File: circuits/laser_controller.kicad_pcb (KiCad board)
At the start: 4 copper layers, 173 x 61.1 mm, 178 parts, among them J1 USB_MINI_B, J2 USB_MINI_B, J5 24V DC IN, J6 CONN_RJ45, Q1 SOT-23, Q2 SOT-23, Q3 SOT-23, Q4 SOT-23, Q5 SOT-23, Q6 SOT-23, SW1 SW_PUSH, SW2 SW_PUSH, SW3 SW_PUSH, U1 SOIC-8_3.9x4.9mm_P1.27mm, U10 QFN-28-1EP_5x5mm_P0.5mm_EP3.3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, U11 SOT-23-5, U12 TSSOP-14_4.4x5mm_P0.65mm, U13 SOT-23, U14 LQFP-64_10x10mm_P0.5mm, U15 TSOT-23-6, U16 TSOT-23-6, U2 SOIC-8_3.9x4.9mm_P1.27mm, U3 SOIC-8_3.9x4.9mm_P1.27mm, U4 SOIC-8_3.9x4.9mm_P1.27mm, U5 SOT-23-5, U6 SOT-23-5, U7 SOT-23-5, U8 SOT-23-5, U9 ESP32-S3-WROOM-1

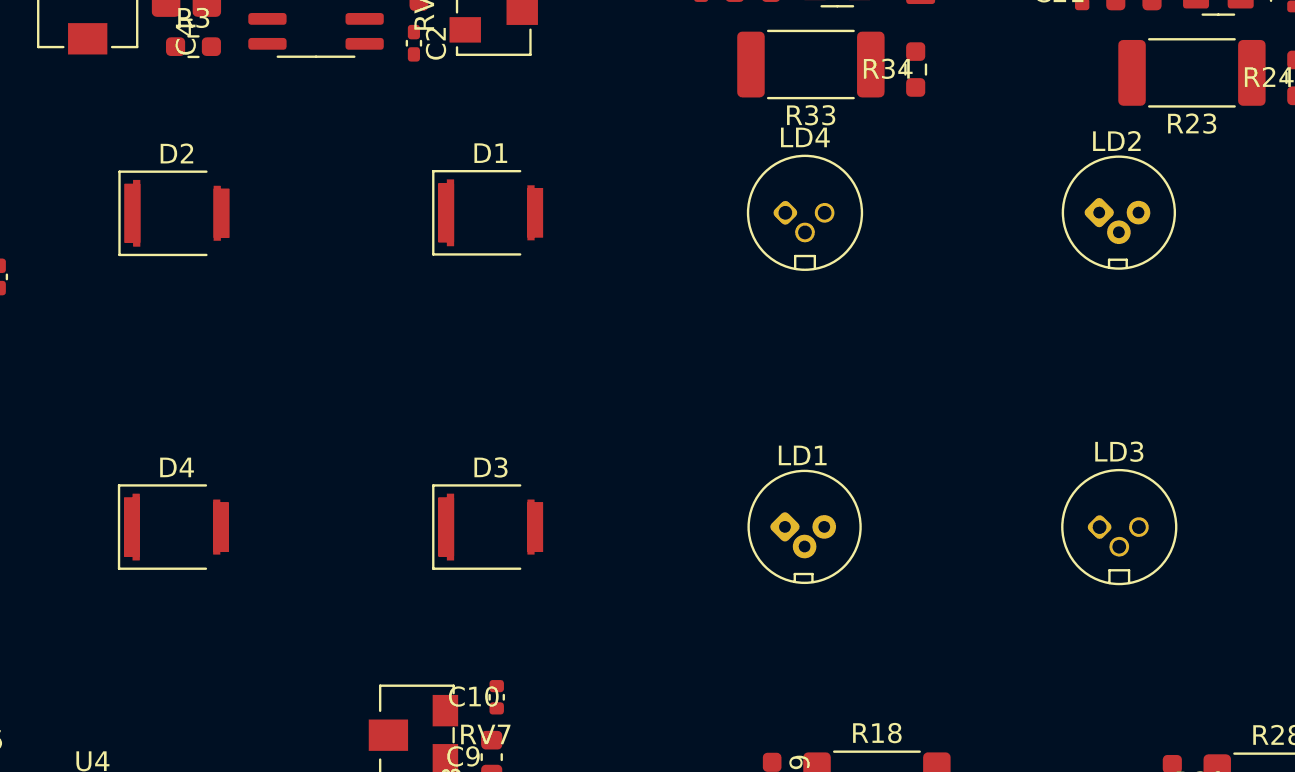
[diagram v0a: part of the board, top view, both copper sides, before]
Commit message: Center PDs and lasers on board Y axis (16mm spacing, symmetric about y=110.44)
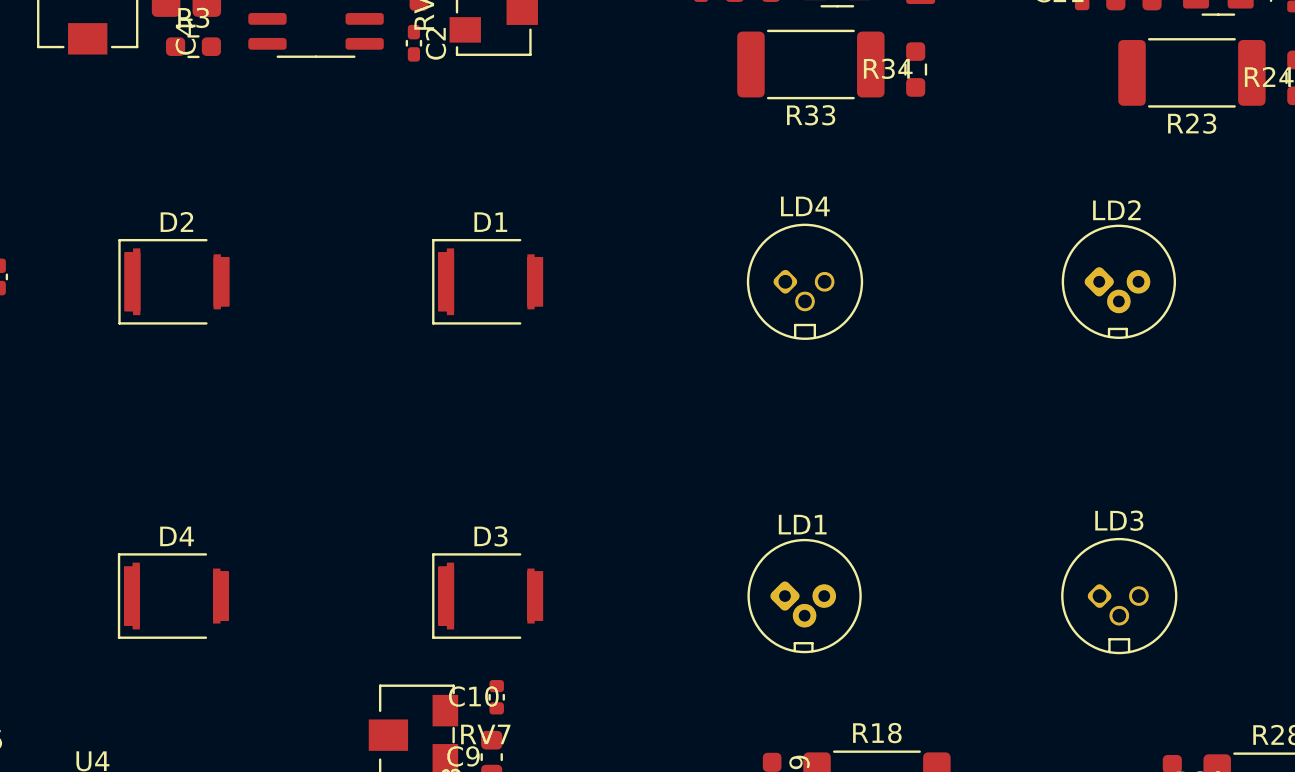
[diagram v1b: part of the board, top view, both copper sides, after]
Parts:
- moved LD1 3.52 mm to (168.9, 118.4)
- moved LD2 3.52 mm to (184.9, 102.4)
- moved D1 3.51 mm to (153.9, 102.4)
- moved D3 3.51 mm to (153.9, 118.4)
- moved D4 3.51 mm to (137.9, 118.4)
- moved LD3 3.51 mm to (184.9, 118.4)
- moved LD4 3.51 mm to (168.9, 102.4)
- moved D2 3.49 mm to (137.9, 102.4)
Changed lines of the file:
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@@
   (net 119 "VOUT4")
   (footprint "Osram_SFH2201" (layer "F.Cu")
-    (at 153.9 98.925)
+    (at 153.9 102.4375)
     (descr "PhotoDiode, Clear Silicone, Osram TOPLED, 4x5.09mm, area: 2.85x2.85mm, Orientation mark at cathode, https://dammedia.osram.info/media/resource/hires/osram-dam-25688470/SFH%202201%20A01_EN.pdf")
     (tags "PhotoDiode silicone")
@@
   )
   (footprint "Osram_SFH2201" (layer "F.Cu")
-    (at 137.925 98.95)
+    (at 137.925 102.4375)
     (descr "PhotoDiode, Clear Silicone, Osram TOPLED, 4x5.09mm, area: 2.85x2.85mm, Orientation mark at cathode, https://dammedia.osram.info/media/resource/hires/osram-dam-25688470/SFH%202201%20A01_EN.pdf")
     (tags "PhotoDiode silicone")
@@
   )
   (footprint "Osram_SFH2201" (layer "F.Cu")
-    (at 153.9 114.925)
+    (at 153.9 118.4375)
     (descr "PhotoDiode, Clear Silicone, Osram TOPLED, 4x5.09mm, area: 2.85x2.85mm, Orientation mark at cathode, https://dammedia.osram.info/media/resource/hires/osram-dam-25688470/SFH%202201%20A01_EN.pdf")
     (tags "PhotoDiode silicone")
@@
   )
   (footprint "Osram_SFH2201" (layer "F.Cu")
-    (at 137.9 114.925)
+    (at 137.9 118.4375)
     (descr "PhotoDiode, Clear Silicone, Osram TOPLED, 4x5.09mm, area: 2.85x2.85mm, Orientation mark at cathode, https://dammedia.osram.info/media/resource/hires/osram-dam-25688470/SFH%202201%20A01_EN.pdf")
     (tags "PhotoDiode silicone")
@@
   )
   (footprint "LaserDiode_TO18-D5.6-3" (layer "F.Cu")
-    (at 168.88 114.915)
+    (at 168.88 118.4375)
     (descr "Laser Diode, TO18-like (D=5.6mm), 3pin")
     (tags "Laser Diode TO18-like")
@@
   )
   (footprint "LaserDiode_TO18-D5.6-3" (layer "F.Cu")
-    (at 184.88 98.915)
+    (at 184.88 102.4375)
     (descr "Laser Diode, TO18-like (D=5.6mm), 3pin")
     (tags "Laser Diode TO18-like")
@@
   )
   (footprint "LaserDiode_TO56-3" (layer "F.Cu")
-    (at 184.9 114.925)
+    (at 184.9 118.4375)
     (descr "Laser Diode, TO-56, 3pin")
     (tags "Laser Diode TO56")
@@
   )
   (footprint "LaserDiode_TO56-3" (layer "F.Cu")
-    (at 168.9 98.925)
+    (at 168.9 102.4375)
     (descr "Laser Diode, TO-56, 3pin")
     (tags "Laser Diode TO56")

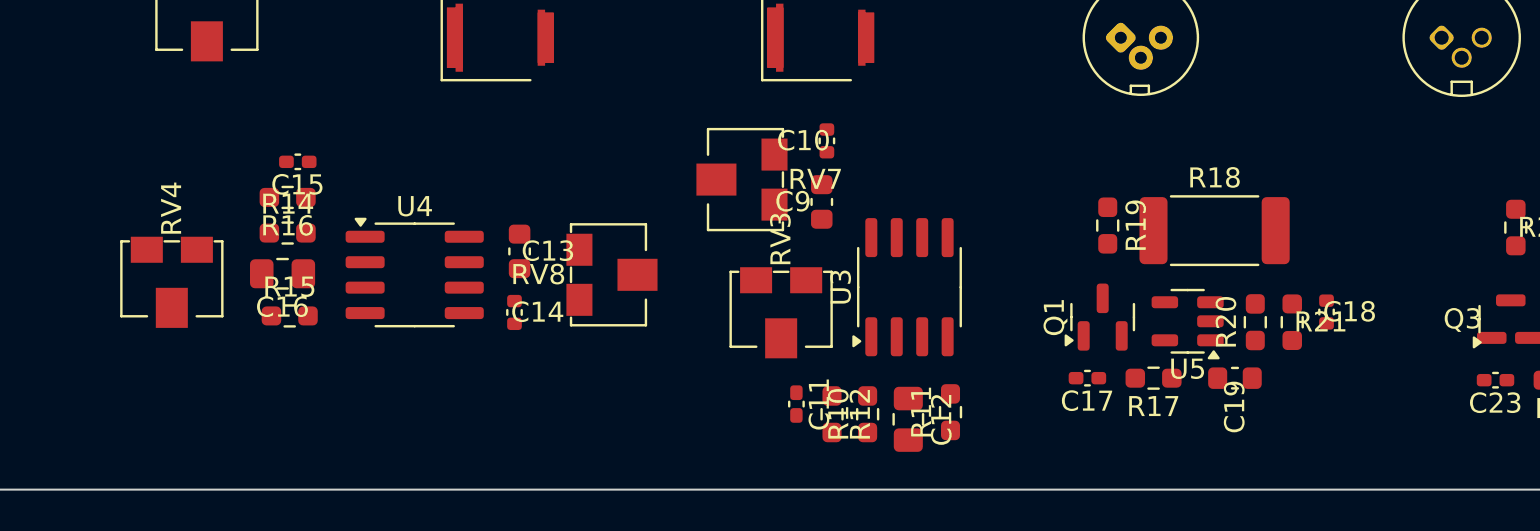
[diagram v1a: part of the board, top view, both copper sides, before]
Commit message: Rotate laser controller backups and sync latest PCB state
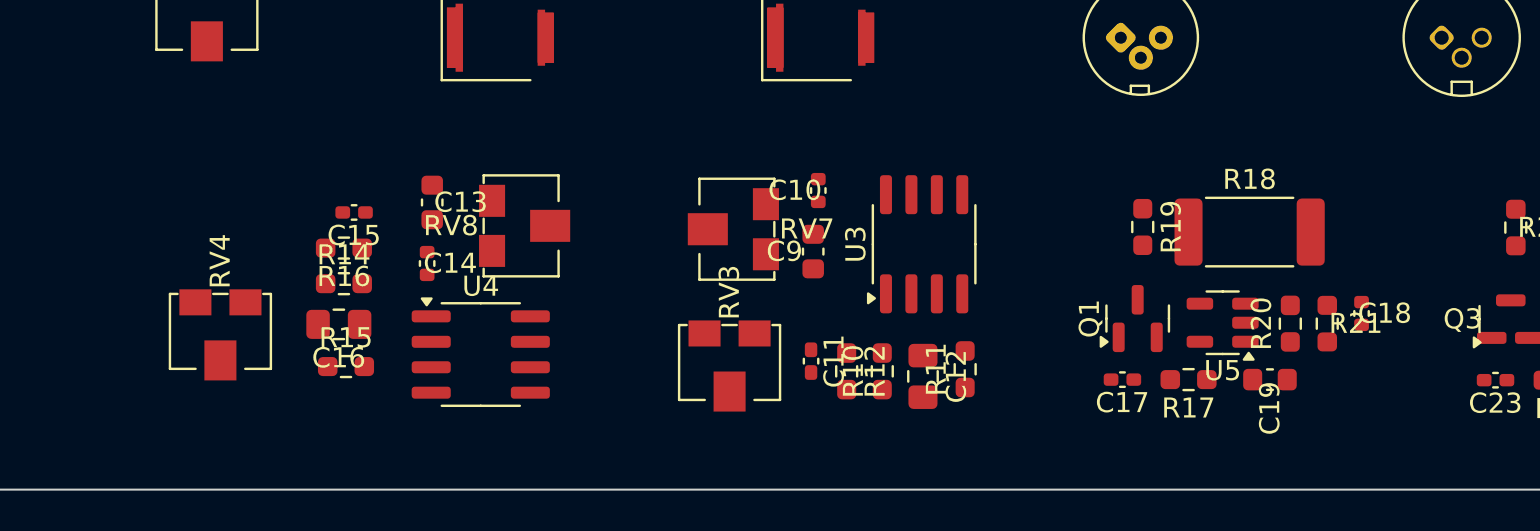
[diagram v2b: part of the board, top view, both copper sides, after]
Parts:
- moved U4 5.17 mm to (136.9, 134.3)
- moved RV8 5.00 mm to (138.9, 127.8)
- moved C13 5.00 mm to (134.5, 126.7)
- moved C14 5.00 mm to (134.2, 129.7)
- moved C15 3.78 mm to (130.6, 127.2)
- moved C16 3.78 mm to (129.8, 132.8)
- moved R14 3.78 mm to (130.1, 130.7)
- moved R16 3.78 mm to (130.1, 128.9)
- moved R15 3.78 mm to (130.2, 134.9)
- moved RV3 3.70 mm to (149.3, 134.7)
- moved RV4 3.57 mm to (123.9, 133.1)
- moved C10 2.51 mm to (153.8, 126.1)
- moved C9 2.51 mm to (153.5, 129.1)
- moved RV7 2.51 mm to (149.7, 128.0)
- moved C11 2.26 mm to (153.4, 134.6)
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
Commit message: Add 3x M3 mounting holes (GND, 3.2mm drill, 7mm pad) for case mounting
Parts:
- added H1: M3, MountingHole_3.2mm_M3, F.Cu at (84.0, 85.0)
- added H2: M3, MountingHole_3.2mm_M3, F.Cu at (197.0, 109.0)
- added H3: M3, MountingHole_3.2mm_M3, F.Cu at (117.0, 136.0)
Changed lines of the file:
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@@
     )
+  )
+  (footprint "MountingHole_3.2mm_M3" (layer "F.Cu")
+    (at 84 85)
+    (attr through_hole)
+    (fp_text reference "H1" (at 0 4.5) (layer "F.SilkS")
+        (effects (font (size 1 1) (thickness 0.15)))
+    )
+    (fp_text value "M3" (at 0 -4.5) (layer "F.Fab")
+        (effects (font (size 1 1) (thickness 0.15)))
+    )
+    (pad "1" thru_hole circle (at 0 0) (size 7 7) (drill 3.2) (layers "*.Cu" "*.Mask")
+      (net 46 "GND"))
+  )
+  (footprint "MountingHole_3.2mm_M3" (layer "F.Cu")
+    (at 197 109)
+    (attr through_hole)
+    (fp_text reference "H2" (at 0 4.5) (layer "F.SilkS")
+        (effects (font (size 1 1) (thickness 0.15)))
+    )
+    (fp_text value "M3" (at 0 -4.5) (layer "F.Fab")
+        (effects (font (size 1 1) (thickness 0.15)))
+    )
+    (pad "1" thru_hole circle (at 0 0) (size 7 7) (drill 3.2) (layers "*.Cu" "*.Mask")
+      (net 46 "GND"))
+  )
+  (footprint "MountingHole_3.2mm_M3" (layer "F.Cu")
+    (at 117 136)
+    (attr through_hole)
+    (fp_text reference "H3" (at 0 4.5) (layer "F.SilkS")
+        (effects (font (size 1 1) (thickness 0.15)))
+    )
+    (fp_text value "M3" (at 0 -4.5) (layer "F.Fab")
+        (effects (font (size 1 1) (thickness 0.15)))
+    )
+    (pad "1" thru_hole circle (at 0 0) (size 7 7) (drill 3.2) (layers "*.Cu" "*.Mask")
+      (net 46 "GND"))
   )
   (gr_line (start 204 141) (end 31 141)

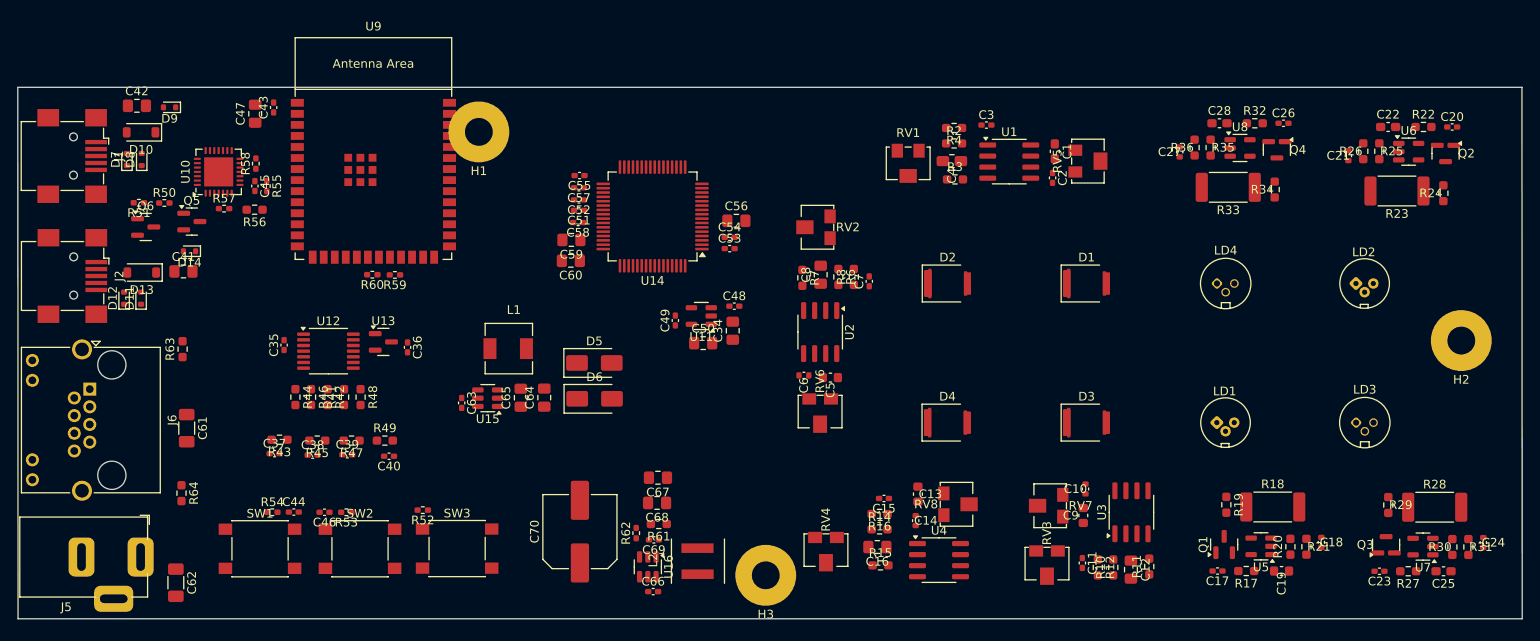
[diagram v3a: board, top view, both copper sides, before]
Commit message: Rotate laser controller backup, sync latest PCB with mounting holes
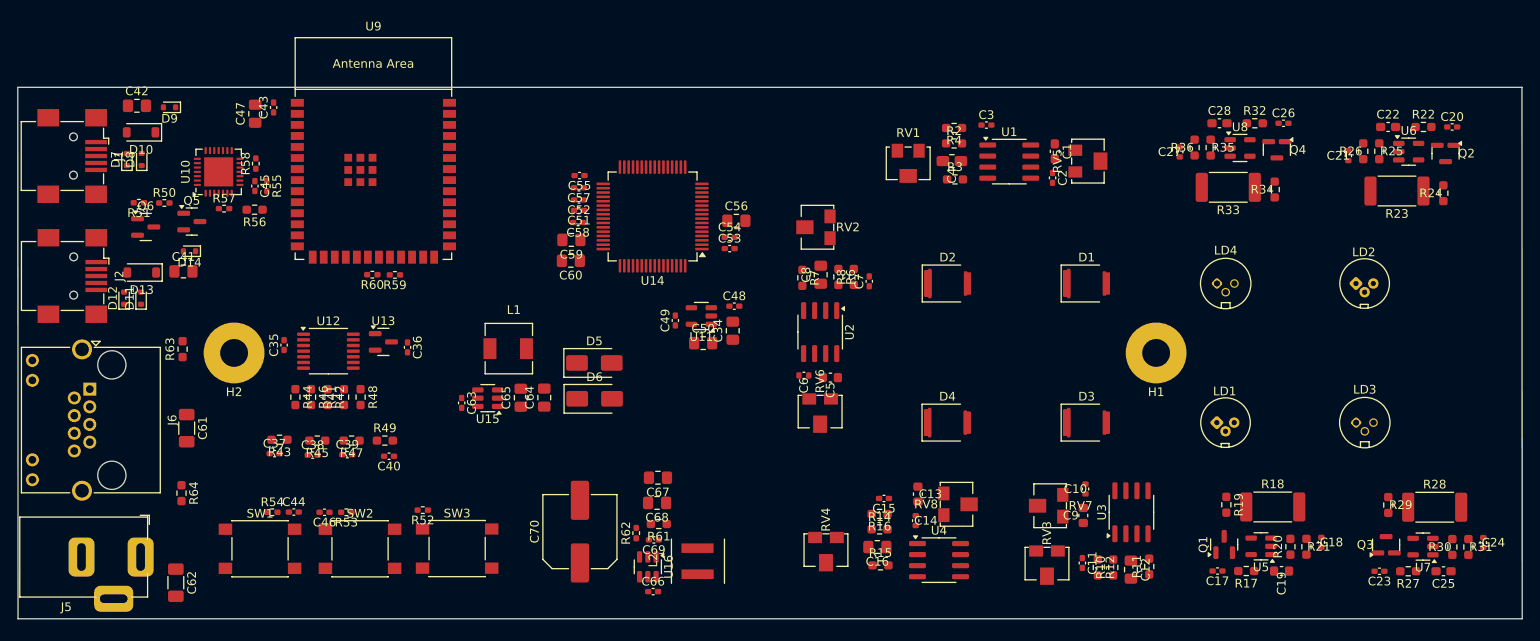
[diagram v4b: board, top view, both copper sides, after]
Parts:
- removed H3: M3, MountingHole_3.2mm_M3
- moved H2 141.2 mm to (55.9, 110.4)
- moved H1 81.9 mm to (161.9, 110.4)
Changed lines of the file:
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@@
   (net 118 "VOUT3")
   (net 119 "VOUT4")
+  (footprint "MountingHole_3.2mm_M3" (layer "F.Cu")
+    (at 161.9 110.425)
+    (attr through_hole)
+    (fp_text reference "H1" (at 0 4.5) (layer "F.SilkS")
+        (effects (font (size 1 1) (thickness 0.15)))
+    )
+    (fp_text value "M3" (at 0 -4.5) (layer "F.Fab")
+        (effects (font (size 1 1) (thickness 0.15)))
+    )
+    (pad "1" thru_hole circle (at 0 0) (size 7 7) (drill 3.2) (layers "*.Cu" "*.Mask")
+      (net 46 "GND"))
+  )
+  (footprint "MountingHole_3.2mm_M3" (layer "F.Cu")
+    (at 55.85 110.425)
+    (attr through_hole)
+    (fp_text reference "H2" (at 0 4.5) (layer "F.SilkS")
+        (effects (font (size 1 1) (thickness 0.15)))
+    )
+    (fp_text value "M3" (at 0 -4.5) (layer "F.Fab")
+        (effects (font (size 1 1) (thickness 0.15)))
+    )
+    (pad "1" thru_hole circle (at 0 0) (size 7 7) (drill 3.2) (layers "*.Cu" "*.Mask")
+      (net 46 "GND"))
+  )
   (footprint "Osram_SFH2201" (layer "F.Cu")
     (at 153.9 102.4375)
@@
     )
   )
-  (footprint "MountingHole_3.2mm_M3" (layer "F.Cu")
-    (at 84 85)
-    (attr through_hole)
-    (fp_text reference "H1" (at 0 4.5) (layer "F.SilkS")
-        (effects (font (size 1 1) (thickness 0.15)))
-    )
-    (fp_text value "M3" (at 0 -4.5) (layer "F.Fab")
-        (effects (font (size 1 1) (thickness 0.15)))
-    )
-    (pad "1" thru_hole circle (at 0 0) (size 7 7) (drill 3.2) (layers "*.Cu" "*.Mask")
-      (net 46 "GND"))
-  )
-  (footprint "MountingHole_3.2mm_M3" (layer "F.Cu")
-    (at 197 109)
-    (attr through_hole)
-    (fp_text reference "H2" (at 0 4.5) (layer "F.SilkS")
-        (effects (font (size 1 1) (thickness 0.15)))
-    )
-    (fp_text value "M3" (at 0 -4.5) (layer "F.Fab")
-        (effects (font (size 1 1) (thickness 0.15)))
-    )
-    (pad "1" thru_hole circle (at 0 0) (size 7 7) (drill 3.2) (layers "*.Cu" "*.Mask")
-      (net 46 "GND"))
-  )
-  (footprint "MountingHole_3.2mm_M3" (layer "F.Cu")
-    (at 117 136)
-    (attr through_hole)
-    (fp_text reference "H3" (at 0 4.5) (layer "F.SilkS")
-        (effects (font (size 1 1) (thickness 0.15)))
-    )
-    (fp_text value "M3" (at 0 -4.5) (layer "F.Fab")
-        (effects (font (size 1 1) (thickness 0.15)))
-    )
-    (pad "1" thru_hole circle (at 0 0) (size 7 7) (drill 3.2) (layers "*.Cu" "*.Mask")
-      (net 46 "GND"))
-  )
   (gr_line (start 204 141) (end 31 141)
